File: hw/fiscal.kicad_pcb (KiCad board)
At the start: 2 copper layers, 101.6 x 50.8 mm, 102 parts, among them J1 35RAPC4BHN2, J2 P1_evens, J3 P2_odds, Q1 2N3904, Q2 2N3904, Q3 2N3904, Q4 2N3904, SW1 SW_DIP_x04, U1 OPA2344, U2 OPA2344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

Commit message: hw: daily release
Signed-off-by: Pau Pajuelo <ppajuel@gmail.com>
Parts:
- added JP3: SolderJumper_3_Open, Jumper:SolderJumper-3_P1.3mm_Open_RoundedPad1.0x1.5mm_NumberLabels, F.Cu at (4.45, 22.9)
- moved C26 253.0 mm to (164.5, 243.2)
- moved C25 243.9 mm to (182.9, 231.1)
- moved R21 156.2 mm to (149.9, -6.35)
- moved C9 155.2 mm to (151.1, 9.53)
- moved D6 128.8 mm to (121.9, 19.1)
- moved R34 123.9 mm to (129.5, 256.5)
- moved C22 122.8 mm to (183.5, 257.2)
- moved R38 120.7 mm to (153.7, 262.9)
- moved C27 118.7 mm to (183.5, 243.8)
- moved R35 116.9 mm to (130.8, 249.6)
- moved R23 115.7 mm to (147.3, 42.4)
- moved R24 115.7 mm to (144.0, 42.4)
- moved C8 113.7 mm to (123.2, 31.1)
- moved R37 110.0 mm to (111.8, 240.0)
- moved R36 109.9 mm to (115.6, 248.9)
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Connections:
- U2 pad 3: PC3_LSin -> Net-(JP3-Pad2)

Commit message: hw: added layout optimizations
-> simplified the number of voltage dividers
-> change lipo footprint

Signed-off-by: Pau Pajuelo <ppajuel@gmail.com>
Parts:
- removed C21, C27: 22u, Capacitor_SMD:CP_Elec_8x6.2
- removed R31, R32: 10K, Resistor_THT:R_Axial_DIN0207_L6.3mm_D2.5mm_P7.62mm_Horizontal
- removed R39, R40: 22K, Resistor_THT:R_Axial_DIN0207_L6.3mm_D2.5mm_P7.62mm_Horizontal
- J1: value 35RAPC4BHN2 -> REF**
- JP1, JP2, JP3: moved to B.Cu
- R16, R18: value 22K -> 10K
- U5: value LF33ABDT -> DPAK
- moved R38 182.3 mm to (225.8, 95.5)
- moved C24 180.1 mm to (215.4, 74.9), turned to 180 degrees
- moved R28 170.5 mm to (124.7, 84.3), turned to 180 degrees
- moved R33 162.1 mm to (140.2, 95.8)
- moved R34 158.8 mm to (147.8, 98.8), turned to 180 degrees
- moved C26 157.7 mm to (221.0, 96.0), turned to 270 degrees
- moved C22 156.4 mm to (143.8, 105.9)
- moved JP3 156.2 mm to (150.1, 79.2)
- moved C25 153.6 mm to (209.0, 79.8), turned to 180 degrees
- moved R27 150.5 mm to (117.1, 87.6), turned to 0 degrees
- moved R35 149.7 mm to (169.2, 104.9), turned to 180 degrees
- moved R26 147.7 mm to (145.3, 78.5), turned to 180 degrees
- moved R36 144.5 mm to (136.4, 105.9), turned to 180 degrees
- moved R43 138.7 mm to (151.9, 96.8), turned to 180 degrees
- moved C20 136.9 mm to (158.2, 96.8)
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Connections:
- C6 pad 1: Net-(C6-Pad1) -> VGND
- R16 pad 1: Net-(C6-Pad1) -> VGND
- R18 pad 1: Net-(C6-Pad1) -> VGND
- U1 pad 3: Net-(C6-Pad1) -> VGND
- U3 pad 3: Net-(C21-Pad1) -> VGND
- U3 pad 5: Net-(C21-Pad1) -> VGND
- U4 pad 5: Net-(C27-Pad1) -> VGND
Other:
- board size 101.6 x 50.8 mm -> 114.3 x 50.8 mm

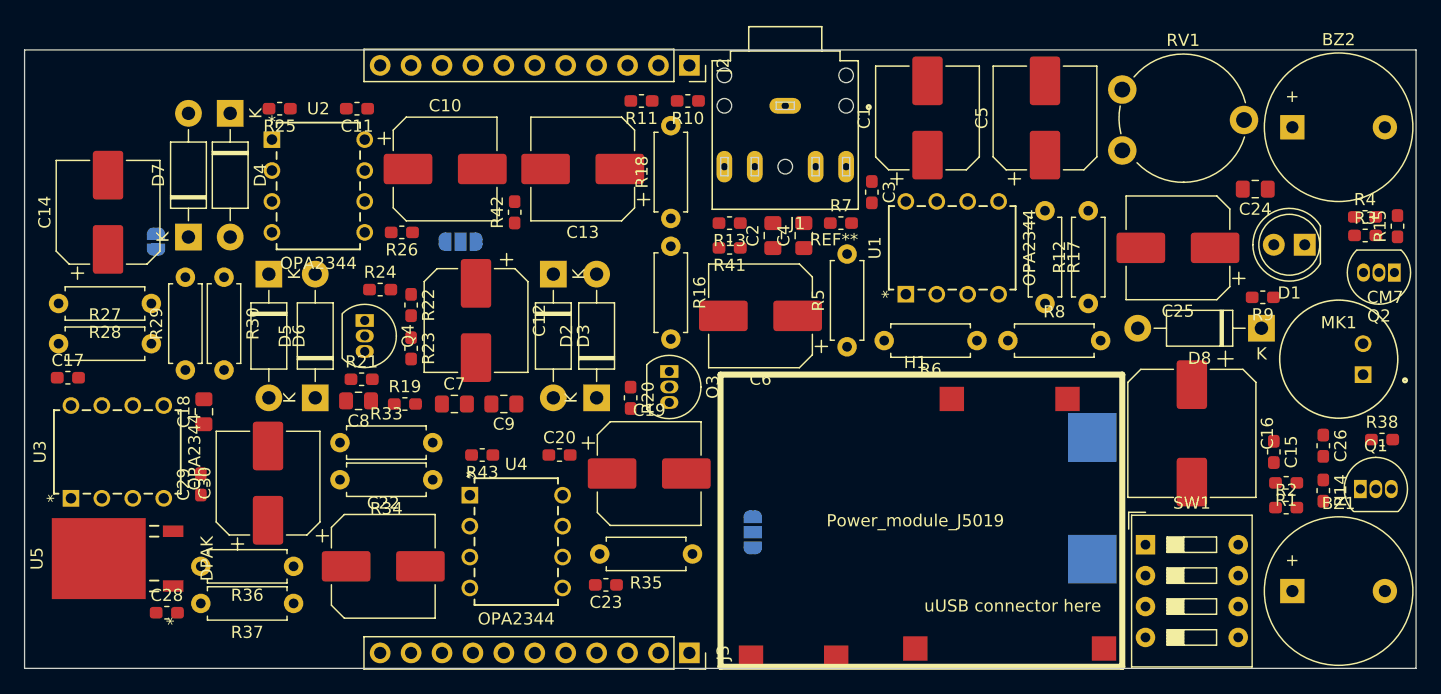
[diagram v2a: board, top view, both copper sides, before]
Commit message: hw: daily release
starting to route layout

Signed-off-by: Pau Pajuelo <ppajuel@gmail.com>
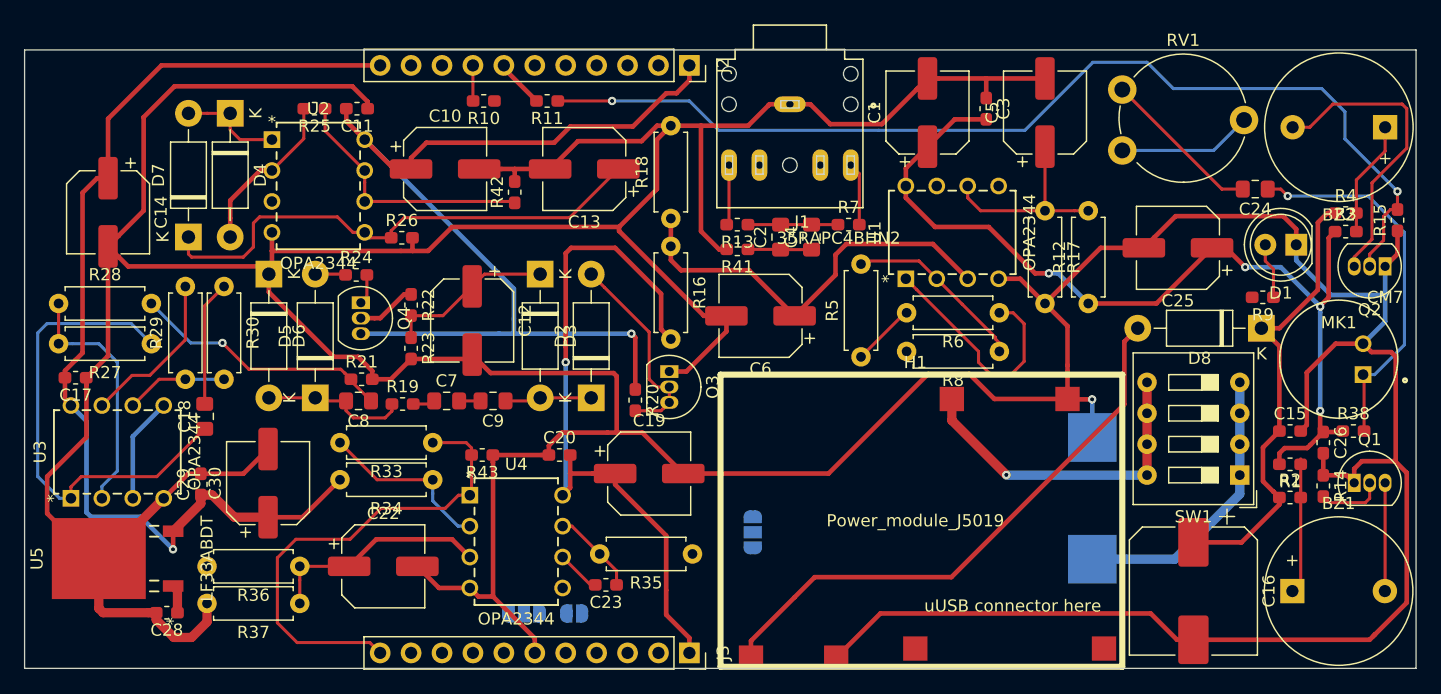
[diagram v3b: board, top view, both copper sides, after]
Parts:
- C1, C10, C12, C13, C14, C19, C22, C25, C30, C5, C6: footprint Capacitor_SMD:CP_Elec_8x6.2 -> Capacitor_SMD:CP_Elec_6.3x5.9
- J1: value REF** -> 35RAPC4BHN2
- U5: value DPAK -> LF33ABDT
- moved JP2 46.0 mm to (159.4, 109.8), turned to 0 degrees
- moved JP3 31.0 mm to (155.3, 109.8), turned to 180 degrees
- moved R10 16.8 mm to (152.0, 67.7)
- moved C16 13.0 mm to (210.3, 108.0)
- moved C3 11.6 mm to (193.3, 68.3)
- moved SW1 9.63 mm to (214.1, 98.4), turned to 180 degrees
- moved R11 7.75 mm to (157.2, 67.7)
- moved BZ2 7.62 mm to (226.1, 69.8), turned to 180 degrees
- moved R27 7.62 mm to (124.7, 87.6), turned to 180 degrees
- moved R28 7.62 mm to (117.1, 84.3), turned to 0 degrees
- moved R33 7.62 mm to (147.8, 95.8), turned to 180 degrees
- moved R6 2.94 mm to (194.4, 85.1)
- moved R25 2.86 mm to (138.1, 68.3)
- moved R38 2.45 mm to (223.5, 94.8)
- moved R24 2.31 mm to (141.5, 82.0)
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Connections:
- R10 pad 2: PE5_Buzzer1 -> PE3_Buzzer2
- R11 pad 2: PE3_Buzzer2 -> PE5_Buzzer1
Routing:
- net GNDD: track 0.00 -> 516.1 mm, vias 0 -> 1
- net +3V3: track 0.00 -> 220.8 mm, vias 0 -> 6
- net +5V: track 0.00 -> 125.0 mm, vias 0 -> 1
- net Net-(Q2-Pad2): track 0.00 -> 85.4 mm, vias 0 -> 2
- net Net-(D8-Pad2): track 0.00 -> 46.6 mm
- net VGND: track 0.00 -> 43.0 mm
- net Net-(C13-Pad1): track 0.00 -> 42.7 mm
- net PA5_VBAT: track 0.00 -> 40.1 mm
- net /AVC_AMP_stg1_out: track 0.00 -> 39.5 mm
- net Net-(C24-Pad1): track 0.00 -> 31.0 mm, vias 0 -> 1
- net VBAT: track 0.00 -> 27.3 mm, vias 0 -> 1
- net Net-(BZ2-Pad2): track 0.00 -> 25.1 mm
- net Net-(BT1-Pad1): track 0.00 -> 23.5 mm
- net Mic_in_AVC_out: track 0.00 -> 21.4 mm, vias 0 -> 1
- net Peak_output: track 0.00 -> 21.3 mm
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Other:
- net class Power added: clearance 0.254, trace_width 0.381, via_dia 0.762, via_drill 0.381
- net class Powerplus added: clearance 0.254, trace_width 0.762, via_dia 1.016, via_drill 0.508

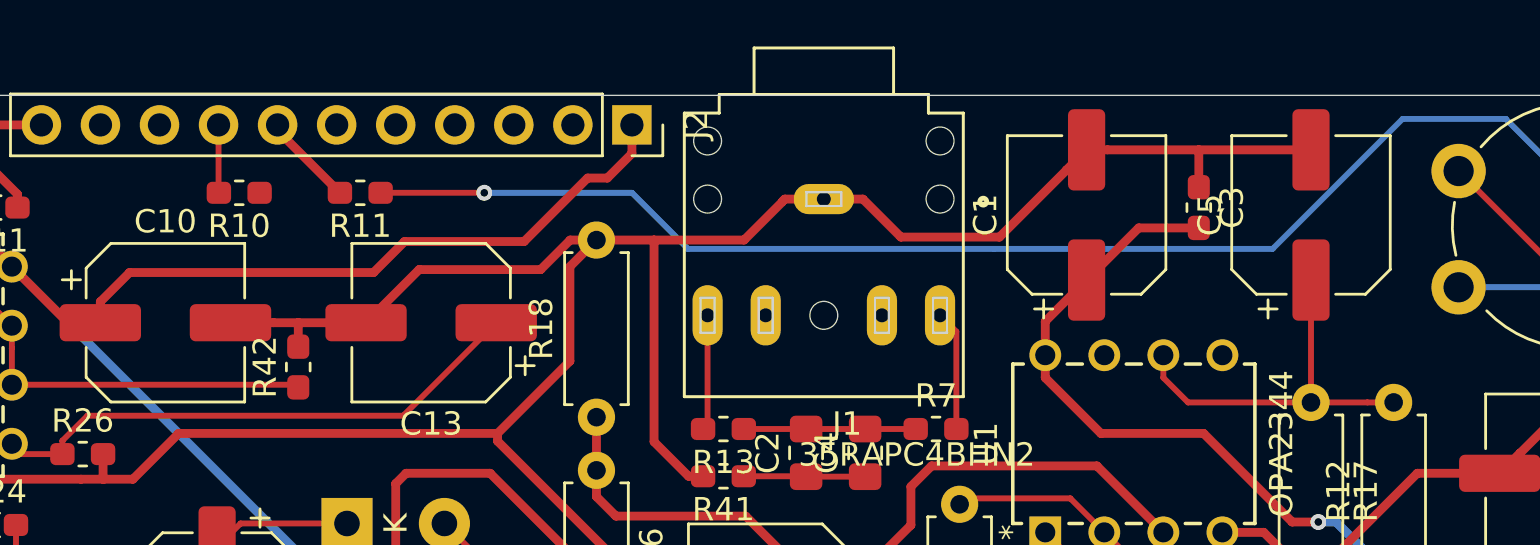
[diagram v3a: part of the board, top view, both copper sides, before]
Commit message: hw: daily release
Added jacksense functionality

Signed-off-by: Pau Pajuelo <ppajuel@gmail.com>
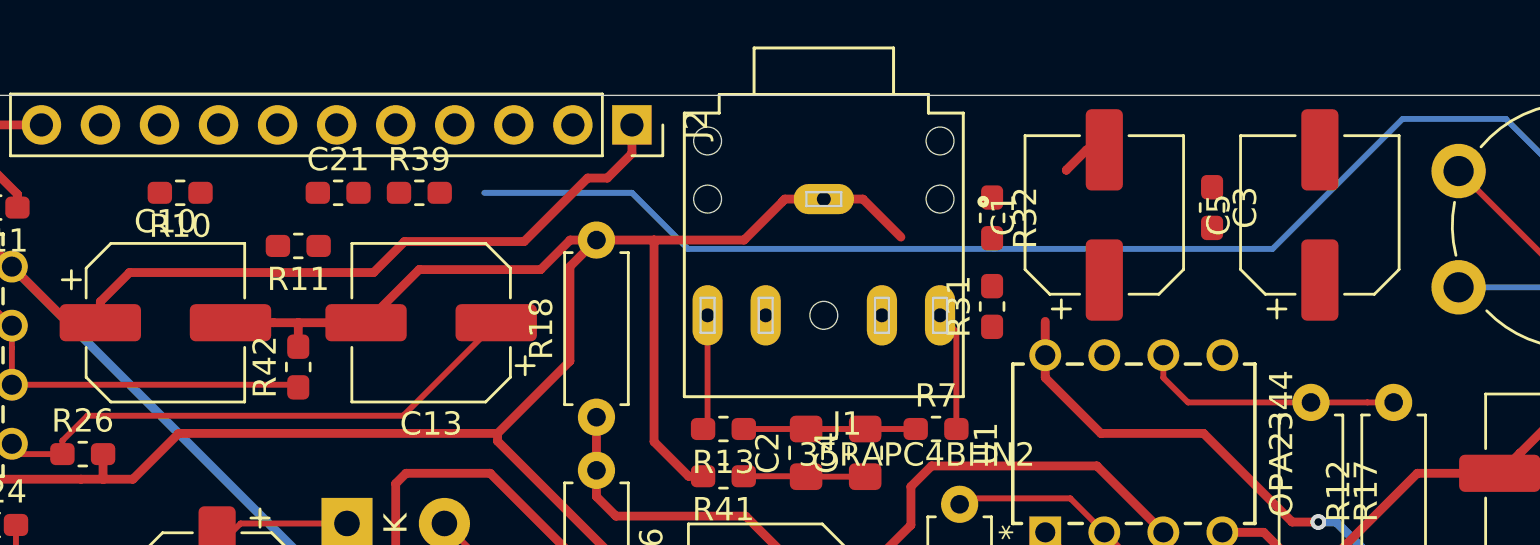
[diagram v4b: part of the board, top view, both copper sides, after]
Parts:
- added C21: 100n, Capacitor_SMD:C_0603_1608Metric_Pad1.05x0.95mm_HandSolder, F.Cu at (156.3, 67.7)
- added R31: 10K, Resistor_SMD:R_0603_1608Metric_Pad1.05x0.95mm_HandSolder, F.Cu at (184.4, 72.6)
- added R32: 100K, Resistor_SMD:R_0603_1608Metric_Pad1.05x0.95mm_HandSolder, F.Cu at (184.4, 68.8)
- added R39: 47K, Resistor_SMD:R_0603_1608Metric_Pad1.05x0.95mm_HandSolder, F.Cu at (159.8, 67.7)
- moved R11 3.51 mm to (154.6, 70.0)
- moved R10 2.54 mm to (149.5, 67.7)
- moved C1 0.76 mm to (189.2, 68.6)
- moved C3 0.57 mm to (193.9, 68.3)
- moved C5 0.38 mm to (198.5, 68.6)
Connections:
- J1 pad 11: Net-(J1-Pad11) -> /JS
- J2 pad 6: Net-(J2-Pad6) -> PC13_Jacksense
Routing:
- net GNDD: track 516.1 -> 497.5 mm
- net +3V3: track 220.8 -> 212.5 mm
- net Net-(C5-Pad1): track 16.6 -> 11.3 mm
- net Net-(Q2-Pad2): track 85.4 -> 81.0 mm, vias 2 -> 1
- net PE5_Buzzer1: track 4.03 -> 0.24 mm
- net PE3_Buzzer2: track 2.93 -> 0.00 mm

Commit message: hw: daily release
Signed-off-by: Pau Pajuelo <ppajuel@gmail.com>
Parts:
- moved JP2 199.1 mm to (168.3, -89.1)
- moved JP3 197.3 mm to (156.3, -87.5)
- moved JP1 191.4 mm to (177.9, -88.2)
- moved R31 3.17 mm to (184.4, 69.4)
- moved R32 2.86 mm to (184.4, 65.9), turned to 90 degrees
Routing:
- net Net-(C23-Pad2): track 16.9 -> 127.4 mm, vias 0 -> 2
- net +5V: track 125.0 -> 230.9 mm, vias 1 -> 4
- net Net-(Q1-Pad2): track 5.45 -> 104.2 mm, vias 0 -> 1
- net VGND: track 43.0 -> 129.7 mm, vias 0 -> 1
- net VBAT: track 27.3 -> 103.5 mm
- net +3V3: track 212.5 -> 286.7 mm
- net Net-(R35-Pad1): track 11.0 -> 71.3 mm, vias 0 -> 2
- net PC3_LSin: track 19.4 -> 73.8 mm, vias 0 -> 1
- net Peak_output: track 21.3 -> 66.9 mm, vias 0 -> 2
- net Net-(R9-Pad2): track 0.00 -> 31.8 mm, vias 0 -> 1
- net /JS: track 0.00 -> 30.8 mm, vias 0 -> 2
- net GNDD: track 497.5 -> 518.6 mm, vias 1 -> 5
- net Net-(C2-Pad1): track 5.23 -> 17.8 mm, vias 0 -> 2
- net Net-(C2-Pad2): track 7.39 -> 17.7 mm
- net Net-(Q2-Pad2): track 81.0 -> 87.1 mm, vias 1 -> 2
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
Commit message: hw: daily release
Signed-off-by: Pau Pajuelo <ppajuel@gmail.com>
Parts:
- added G***: LOGO, kicad-lib:fiscal-logo, B.Cu at (152.0, 75.0)
- J1: value 35RAPC4BHN2 -> (none)
- MK1: value CM7 -> (none)
- U1, U2, U3, U4: value OPA2344 -> (none)
- U5: value LF33ABDT -> (none)
- moved JP2 191.6 mm to (143.2, 100.8)
- moved JP3 191.3 mm to (153.4, 103.8), turned to 270 degrees
- moved JP1 190.7 mm to (156.0, 101.2)
- moved BZ2 7.62 mm to (218.4, 69.8), turned to 0 degrees
- moved C20 1.27 mm to (158.2, 95.5)
- moved R43 1.27 mm to (151.9, 95.5)
- moved J1 0.15 mm to (177.2, 68.8)
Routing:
- net PF6_MICin: track 0.00 -> 46.7 mm, vias 0 -> 2
- net Net-(JP3-Pad2): track 0.00 -> 44.0 mm, vias 0 -> 4
- net Net-(JP2-Pad1): track 13.5 -> 38.7 mm, vias 0 -> 1
- net /AVC_AMP_stg1_out: track 39.5 -> 23.1 mm, vias 0 -> 2
- net GNDD: track 518.6 -> 534.6 mm, vias 5 -> 30
- net Net-(BZ2-Pad2): track 25.1 -> 12.5 mm
- net Net-(C7-Pad2): track 1.76 -> 11.8 mm, vias 0 -> 1
- net Mic_in_analog: track 7.11 -> 10.2 mm
- net +3V3: track 286.7 -> 283.9 mm
- net Net-(C23-Pad2): track 127.4 -> 125.3 mm
- net Net-(BZ2-Pad1): track 9.55 -> 11.5 mm
- net PC3_LSin: track 73.8 -> 75.0 mm
- net VBAT: track 103.5 -> 104.5 mm
- net PA5_VBAT: track 40.1 -> 40.9 mm
- net Net-(R33-Pad2): track 14.5 -> 14.9 mm, vias 0 -> 1
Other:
- board size 114.3 x 50.8 mm -> 113 x 50.8 mm
- board text added: "FISCAL Exp. 2019 ver: 1 ppajuel"

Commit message: hw: daily release
Signed-off-by: Pau Pajuelo <ppajuel@gmail.com>
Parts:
- moved G*** 3.16 mm to (150.4, 72.3)
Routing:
- net +5V: track 230.9 -> 210.2 mm
- net Net-(C23-Pad2): track 125.3 -> 110.8 mm
- net PC3_LSin: track 75.0 -> 60.5 mm
- net Net-(R35-Pad1): track 71.3 -> 66.0 mm, vias 2 -> 1
- net GNDD: track 534.6 -> 538.3 mm
- net Net-(C13-Pad1): track 42.7 -> 40.7 mm
- net +3V3: track 283.9 -> 286.0 mm
- net VBAT: track 104.5 -> 102.6 mm
- net Net-(D8-Pad2): track 48.3 -> 46.6 mm
- net PF6_MICin: track 46.7 -> 48.4 mm
- net Net-(JP3-Pad2): track 44.0 -> 42.9 mm
- net Net-(C7-Pad2): track 11.8 -> 12.5 mm
- net /Fdbck_ppp: track 13.6 -> 13.0 mm
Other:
- board text added: "Battery placement"
- board text added: "Oh, by the way, which one's Pink?"

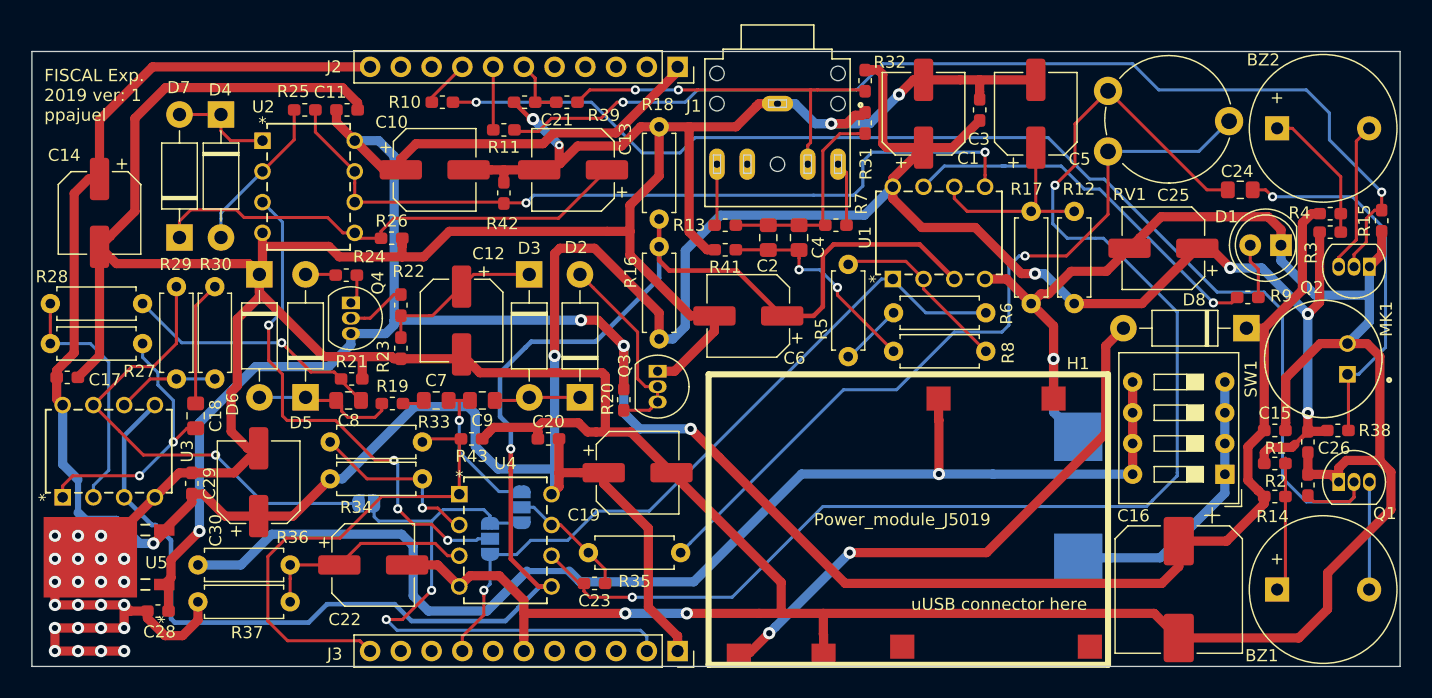
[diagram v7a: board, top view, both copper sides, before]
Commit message: hw: added layout DGND copper pours
Signed-off-by: Pau Pajuelo <ppajuel@gmail.com>
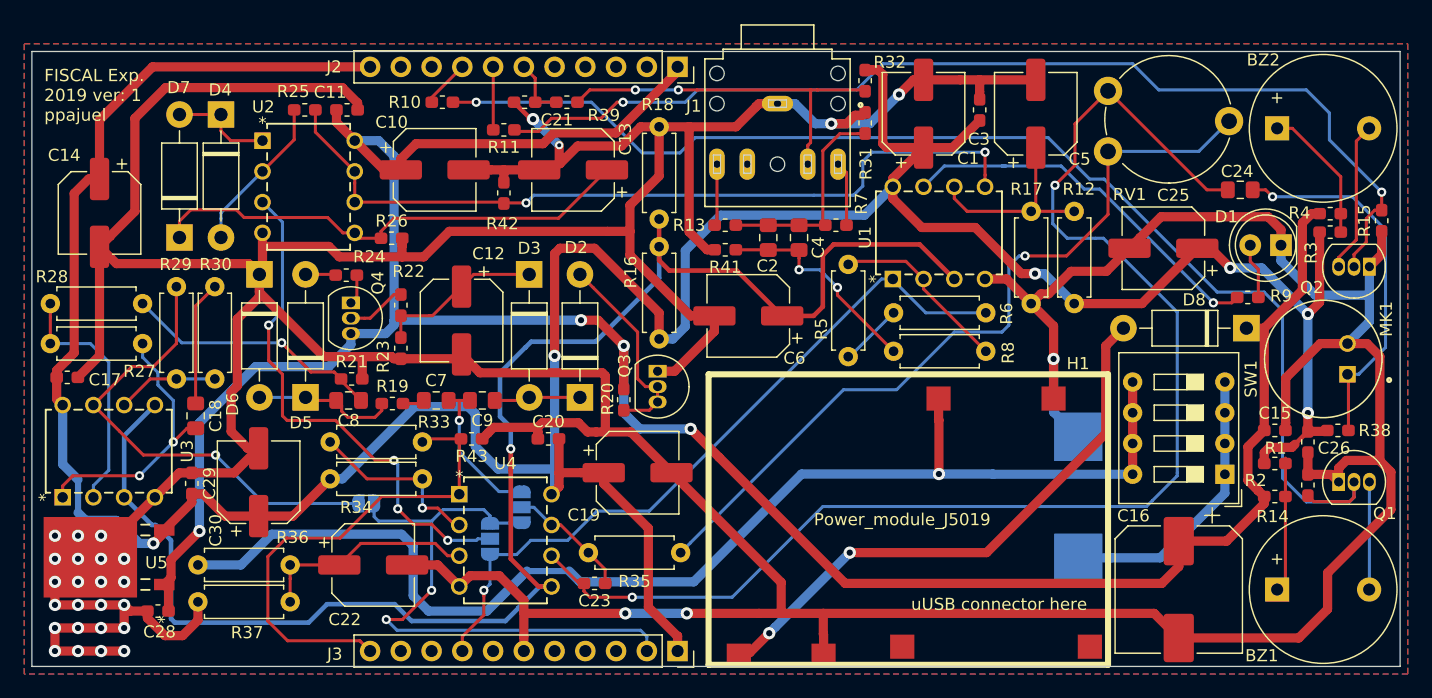
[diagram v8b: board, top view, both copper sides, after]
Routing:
- added copper zone on B.Cu, net GNDD
- added copper zone on F.Cu, net GNDD
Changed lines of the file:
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@@
     (tags "resistor handsolder")
     (attr smd)
-    (fp_text reference R2 (at 0.0635 -1.27) (layer F.SilkS)
+    (fp_text reference R2 (at -1.5875 -1.3335) (layer F.SilkS)
       (effects (font (size 1 1) (thickness 0.15)))
     )
@@
   (segment (start 157.1485 67.691) (end 157.1485 65.7085) (width 0.254) (layer F.Cu) (net 70))
   (segment (start 157.1485 67.691) (end 158.891 67.691) (width 0.254) (layer F.Cu) (net 70))
+  (zone (net 2) (net_name GNDD) (layer F.Cu) (hatch edge 0.508)
+    (connect_pads (clearance 0.508))
+    (min_thickness 0.254)
+    (fill yes (arc_segments 16) (thermal_gap 0.508) (thermal_bridge_width 0.508))
+    (polygon
+      (pts
+        (xy 114.935 114.935) (xy 114.935 62.865) (xy 229.235 62.865) (xy 229.235 114.935)
+      )
+    )
+  )
+  (zone (net 2) (net_name GNDD) (layer B.Cu) (hatch edge 0.508)
+    (connect_pads (clearance 0.508))
+    (min_thickness 0.254)
+    (fill yes (arc_segments 16) (thermal_gap 0.508) (thermal_bridge_width 0.508))
+    (polygon
+      (pts
+        (xy 114.935 114.935) (xy 114.935 62.865) (xy 229.235 62.865) (xy 229.235 114.935)
+      )
+    )
+  )
 )
